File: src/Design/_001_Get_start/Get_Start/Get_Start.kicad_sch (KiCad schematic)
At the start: 7 parts, among them SW1 SW_SPST

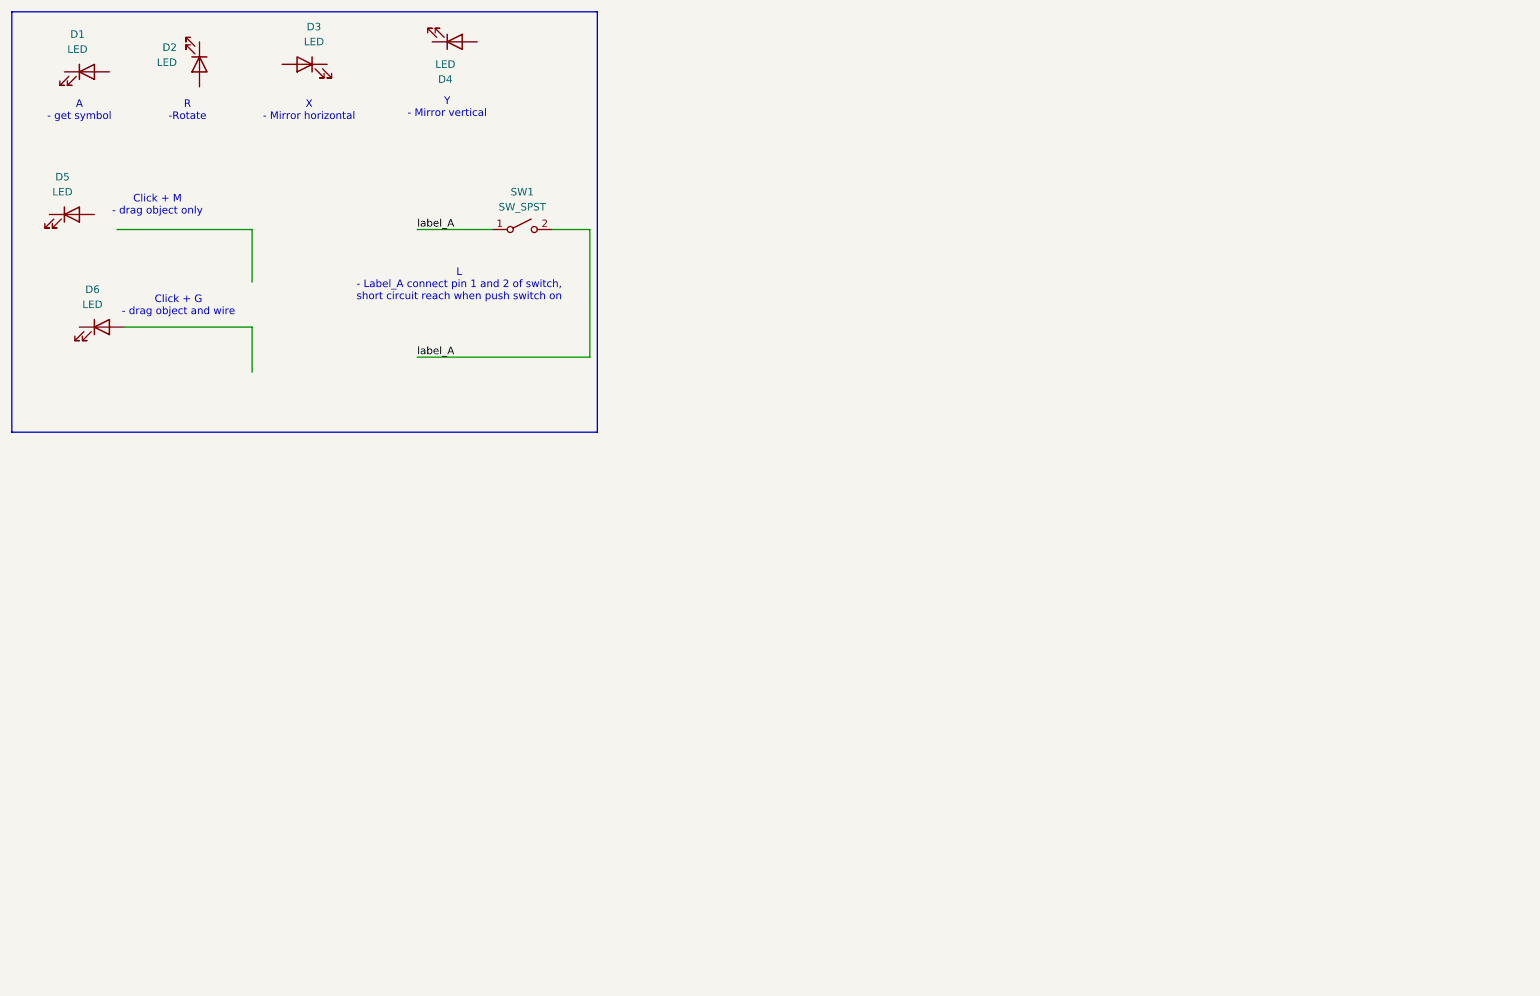
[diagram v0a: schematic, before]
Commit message: :bookmark_tabs: Note something schematic - 001: special connect hierarchy of sheets - 003: Set properties for symbols - 004: error rule check for schematic
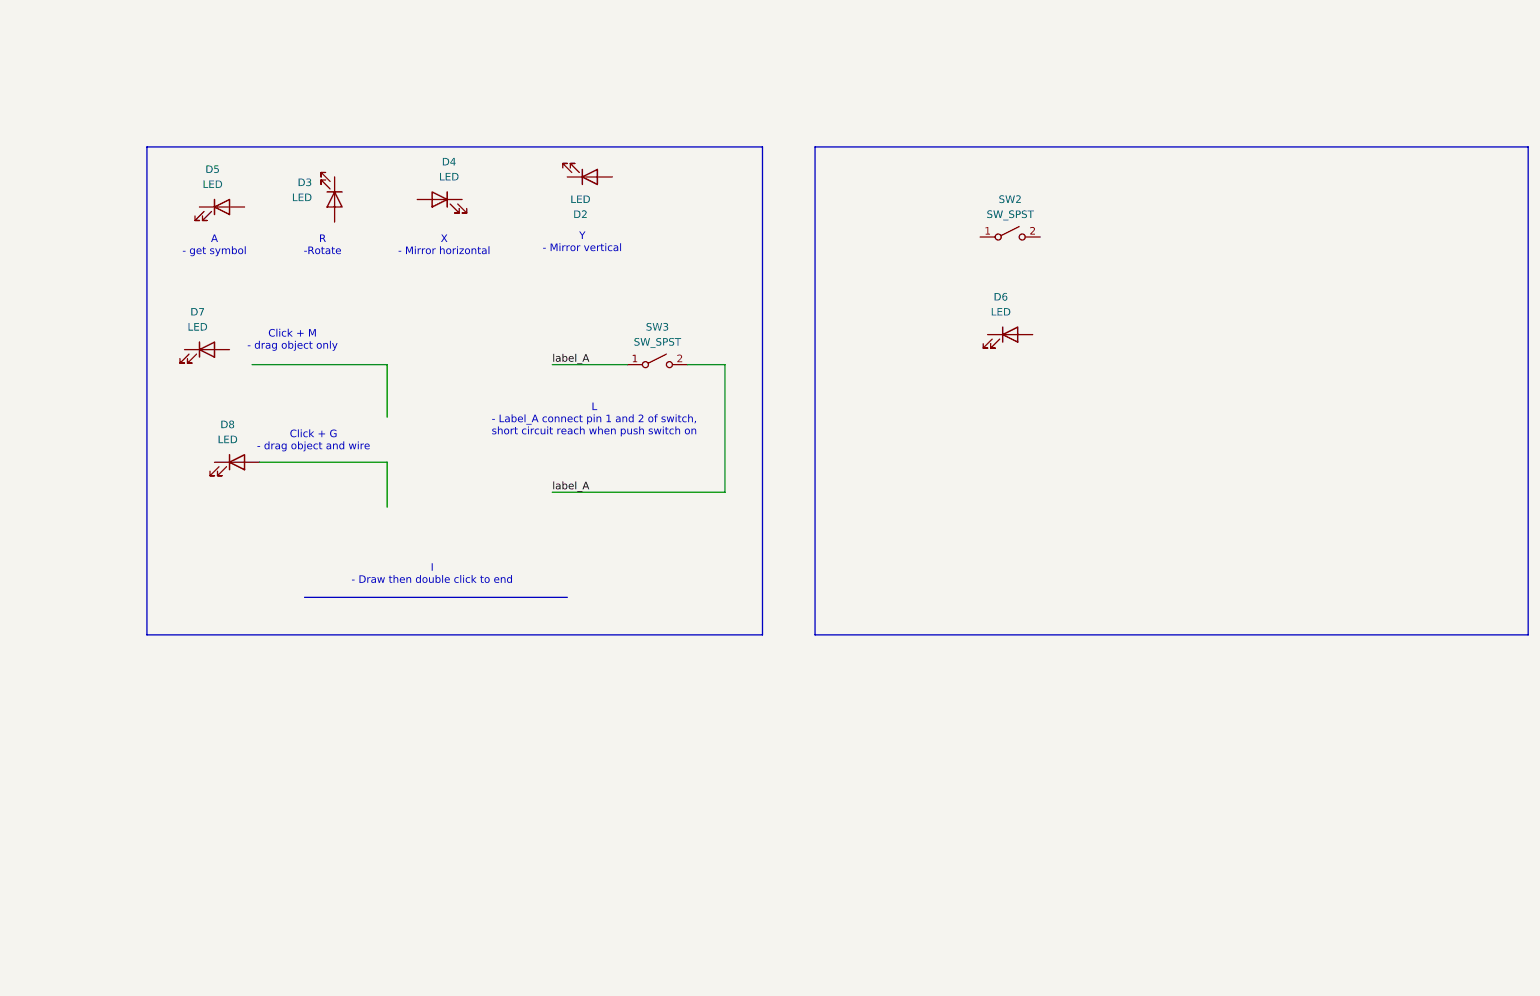
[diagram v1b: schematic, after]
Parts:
- added D6: LED, symbol Device:LED
- added SW2: SW_SPST, symbol Switch:SW_SPST
- renumbered D4 to D2, D2 to D3, D3 to D4, D1 to D5, D5 to D7, D6 to D8, SW1 to SW3
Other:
- note added: "I - Draw then double click to end"
- moved on the sheet: D2, D3, D4, D5, D7, D8, SW3

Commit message: update
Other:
- added sheet Sheet child 1 (Sheet_child_1.kicad_sch)
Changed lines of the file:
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@@
-		)
-	)
-	(rule_area
-		(polyline
-			(pts
-				(xy 246.38 43.18) (xy 215.9 43.18) (xy 215.9 62.23) (xy 223.52 69.85) (xy 243.84 69.85) (xy 251.46 62.23)
-				(xy 251.46 48.26)
-			)
-			(stroke
-				(width 0)
-				(type dash)
-			)
-			(fill
-				(type none)
-			)
 		)
 	)
@@
 				)
 			)
+		)
+	)
+	(sheet
+		(at 36.83 137.16)
+		(size 49.53 33.02)
+		(exclude_from_sim no)
+		(in_bom yes)
+		(on_board yes)
+		(dnp no)
+		(fields_autoplaced yes)
+		(stroke
+			(width 0.1524)
+			(type solid)
+		)
+		(fill
+			(color 0 0 0 0.0000)
+		)
+		(property "Sheetname" "Sheet child 1"
+			(at 36.83 136.4484 0)
+			(effects
+				(font
+					(size 1.27 1.27)
+				)
+				(justify left bottom)
+			)
+		)
+		(property "Sheetfile" "Sheet_child_1.kicad_sch"
+			(at 36.83 170.7646 0)
+			(effects
+				(font
+					(size 1.27 1.27)
+				)
+				(justify left top)
+			)
+		)
+		(pin "hierar_1" input
+			(at 86.36 143.51 0)
+			(effects
+				(font
+					(size 1.27 1.27)
+				)
+				(justify right)
+			)
+		)
+		(pin "hierar_2" input
+			(at 74.93 170.18 270)
+			(effects
+				(font
+					(size 1.27 1.27)
+				)
+				(justify left)
+			)
+		)
+		(instances
+			(project "Get_Start"
+				(path "/3c26b505-18dc-433f-8569-20dcedbd6448"
+					(page "2")
+				)
+			)

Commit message: reup
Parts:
- removed D6: LED, symbol Device:LED
- removed SW2: SW_SPST, symbol Switch:SW_SPST
- added D5: LED, symbol Device:LED
- renumbered D2 to D1, D3 to D2, D4 to D3, D5 to D4, D7 to D6, D8 to D7, SW3 to SW1
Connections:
- new net null: D5.1 (K), D5.2 (A)
- no-connect marks 0 -> 16
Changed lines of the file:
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@@
+		)
+	)
+	(no_connect
+		(at 106.68 40.64)
+	)
+	(no_connect
+		(at 67.31 48.26)
+	)
+	(no_connect
+		(at 76.2 96.52)
+	)
+	(no_connect
+		(at 81.28 44.45)
+	)
+	(no_connect
+		(at 52.07 45.72)
+	)
+	(no_connect
+		(at 53.34 72.39)
+	)
+	(no_connect
+		(at 67.31 40.64)
+	)
+	(no_connect
+		(at 49.53 69.85)
+	)
+	(no_connect
+		(at 114.3 40.64)
+	)
+	(no_connect
+		(at 44.45 45.72)
+	)
+	(no_connect
+		(at 41.91 69.85)
+	)
+	(no_connect
+		(at 88.9 44.45)
+	)
+	(no_connect
+		(at 46.99 88.9)
+	)
+	(no_connect
+		(at 76.2 81.28)
+	)
+	(no_connect
+		(at 92.71 143.51)
+	)
+	(no_connect
+		(at 74.93 176.53)
+	)
+	(wire
+		(pts
+			(xy 165.1 50.8) (xy 168.91 50.8)
+		)
+		(stroke
+			(width 0)
+			(type default)
+		)
+	)
+	(wire
+		(pts
+			(xy 74.93 170.18) (xy 74.93 176.53)
+		)
+		(stroke
+			(width 0)
+			(type default)
 		)
 	)
@@
 	(wire
 		(pts
+			(xy 176.53 50.8) (xy 179.07 50.8)
+		)
+		(stroke
+			(width 0)
+			(type default)
+		)
+	)
+	(wire
+		(pts
 			(xy 133.35 93.98) (xy 133.35 72.39)
 		)
@@
 	(wire
 		(pts
+			(xy 86.36 143.51) (xy 92.71 143.51)
+		)
+		(stroke
+			(width 0)
+			(type default)
+		)
+	)
+	(wire
+		(pts
 			(xy 104.14 72.39) (xy 116.84 72.39)
 		)
@@
 			(width 0)
 			(type default)
+		)
+	)
+	(label "null2"
+		(at 76.2 76.2 0)
+		(effects
+			(font
+				(size 1.27 1.27)
+			)
+			(justify left bottom)
+		)
+	)
+	(label "null"
+		(at 179.07 50.8 0)
+		(effects
+			(font
+				(size 1.27 1.27)
+			)
+			(justify left bottom)
+		)
+	)
+	(label "null"
+		(at 57.15 72.39 0)
+		(effects
+			(font
+				(size 1.27 1.27)
+			)
+			(justify left bottom)
 		)
 	)
@@
 			)
 			(justify left bottom)
+		)
+	)
+	(label "null2"
+		(at 165.1 50.8 180)
+		(effects
+			(font
+				(size 1.27 1.27)
+			)
+			(justify right bottom)
 		)
 	)
@@
 		(on_board yes)
 		(dnp no)
-		(property "Reference" "D3"
+		(property "Reference" "D2"
 			(at 63.5 41.5924 90)
 			(effects
@@
 			(project ""
 				(path "/3c26b505-18dc-433f-8569-20dcedbd6448"
-					(reference "D3")
+					(reference "D2")
 					(unit 1)
 				)
@@
 		(on_board yes)
 		(dnp no)
-		(property "Reference" "D4"
+		(property "Reference" "D3"
 			(at 86.6775 38.1 0)
 			(effects
@@
 			(project ""
 				(path "/3c26b505-18dc-433f-8569-20dcedbd6448"
-					(reference "D4")
+					(reference "D3")
 					(unit 1)
 				)
@@
 		(on_board yes)
 		(dnp no)
-		(fields_autoplaced yes)
-		(property "Reference" "D8"
+		(property "Reference" "D7"
 			(at 49.2125 82.55 0)
 			(effects
@@
 			(project ""
 				(path "/3c26b505-18dc-433f-8569-20dcedbd6448"
-					(reference "D8")
+					(reference "D7")
 					(unit 1)
 				)
@@
 		(on_board yes)
 		(dnp no)
-		(property "Reference" "D2"
+		(property "Reference" "D1"
 			(at 108.9025 46.99 0)
 			(effects
@@
 			(project "Get_Start"
 				(path "/3c26b505-18dc-433f-8569-20dcedbd6448"
-					(reference "D2")
+					(reference "D1")
 					(unit 1)
 				)
@@
 		(dnp no)
 		(fields_autoplaced yes)
-		(property "Reference" "D7"
+		(property "Reference" "D6"
 			(at 44.1325 63.5 0)
 			(effects
@@
 			(project ""
 				(path "/3c26b505-18dc-433f-8569-20dcedbd6448"
-					(reference "D7")
+					(reference "D6")
+					(unit 1)
+				)
+			)
+		)
+	)
+	(symbol
+		(lib_id "Device:LED")
+		(at 172.72 50.8 0)
+		(unit 1)
+		(exclude_from_sim no)
+		(in_bom yes)
+		(on_board yes)
+		(dnp no)
+		(fields_autoplaced yes)
+		(property "Reference" "D5"
+			(at 171.1325 44.45 0)
+			(effects
+				(font
+					(size 1.27 1.27)
+				)
+			)
+		)
+		(property "Value" "LED"
+			(at 171.1325 46.99 0)
+			(effects
+				(font
+					(size 1.27 1.27)
+				)
+			)
+		)
+		(property "Footprint" ""
+			(at 172.72 50.8 0)
+			(effects
+				(font
+					(size 1.27 1.27)
+				)
+				(hide yes)
+			)
+		)
+		(property "Datasheet" "~"
+			(at 172.72 50.8 0)
+			(effects
+				(font
+					(size 1.27 1.27)
+				)
+				(hide yes)
+			)
+		)
+		(property "Description" "Light emitting diode"
+			(at 172.72 50.8 0)
+			(effects
+				(font
+					(size 1.27 1.27)
+				)
+				(hide yes)
+			)
+		)
+		(property "Sim.Pins" "1=K 2=A"
+			(at 172.72 50.8 0)
+			(effects
+				(font
+					(size 1.27 1.27)
+				)
+				(hide yes)
+			)
+		)
+		(pin "2"
+		)
+		(pin "1"
+		)
+		(instances
+			(project ""
+				(path "/3c26b505-18dc-433f-8569-20dcedbd6448"
+					(reference "D5")
 					(unit 1)
 				)
@@
 		(dnp no)
 		(fields_autoplaced yes)
-		(property "Reference" "D5"
+		(property "Reference" "D4"
 			(at 46.6725 39.37 0)
 			(effects
@@
 			(project ""
 				(path "/3c26b505-18dc-433f-8569-20dcedbd6448"
-					(reference "D5")
+					(reference "D4")
 					(unit 1)
 				)
@@
 		(dnp no)
 		(fields_autoplaced yes)
-		(property "Reference" "SW3"
+		(property "Reference" "SW1"
 			(at 121.92 66.04 0)
 			(effects
@@
 			(project ""
 				(path "/3c26b505-18dc-433f-8569-20dcedbd6448"
-					(reference "SW3")
-					(unit 1)
-				)
-			)
-		)
-	)
-	(symbol
-		(lib_id "Device:LED")
-		(at 181.61 67.31 0)
-		(unit 1)
-		(exclude_from_sim no)
-		(in_bom yes)
-		(on_board yes)
-		(dnp no)
-		(fields_autoplaced yes)
-		(property "Reference" "D6"
-			(at 180.0225 60.96 0)
-			(effects
-				(font
-					(size 1.27 1.27)
-				)
-			)
-		)
-		(property "Value" "LED"
-			(at 180.0225 63.5 0)
-			(effects
-				(font
-					(size 1.27 1.27)
-				)
-			)
-		)
-		(property "Footprint" ""
-			(at 181.61 67.31 0)
-			(effects
-				(font
-					(size 1.27 1.27)
-				)
-				(hide yes)
-			)
-		)
-		(property "Datasheet" "~"
-			(at 181.61 67.31 0)
-			(effects
-				(font
-					(size 1.27 1.27)
-				)
-				(hide yes)
-			)
-		)
-		(property "Description" "Light emitting diode"
-			(at 181.61 67.31 0)
-			(effects
-				(font
-					(size 1.27 1.27)
-				)
-				(hide yes)
-			)
-		)
-		(property "Sim.Pins" "1=K 2=A"
-			(at 181.61 67.31 0)
-			(effects
-				(font
-					(size 1.27 1.27)
-				)
-				(hide yes)
-			)
-		)
-		(pin "1"
-		)
-		(pin "2"
-		)
-		(instances
-			(project ""
-				(path "/3c26b505-18dc-433f-8569-20dcedbd6448"
-					(reference "D6")
-					(unit 1)
-				)
-			)
-		)
-	)
-	(symbol
-		(lib_id "Switch:SW_SPST")
-		(at 181.61 50.8 0)
-		(unit 1)
-		(exclude_from_sim no)
-		(in_bom yes)
-		(on_board yes)
-		(dnp no)
-		(fields_autoplaced yes)
-		(property "Reference" "SW2"
-			(at 181.61 44.45 0)
-			(effects
-				(font
-					(size 1.27 1.27)
-				)
-			)
-		)
-		(property "Value" "SW_SPST"
-			(at 181.61 46.99 0)
-			(effects
-				(font
-					(size 1.27 1.27)
-				)
-			)
-		)
-		(property "Footprint" ""
-			(at 181.61 50.8 0)
-			(effects
-				(font
-					(size 1.27 1.27)
-				)
-				(hide yes)
-			)
-		)
-		(property "Datasheet" "~"
-			(at 181.61 50.8 0)
-			(effects
-				(font
-					(size 1.27 1.27)
-				)
-				(hide yes)
-			)
-		)
-		(property "Description" "Single Pole Single Throw (SPST) switch"
-			(at 181.61 50.8 0)
-			(effects
-				(font
-					(size 1.27 1.27)
-				)
-				(hide yes)
-			)
-		)
-		(pin "1"
-		)
-		(pin "2"
-		)
-		(instances
-			(project ""
-				(path "/3c26b505-18dc-433f-8569-20dcedbd6448"
-					(reference "SW2")
+					(reference "SW1")
 					(unit 1)
 				)
@@
 			)
 		)
-		(pin "hierar_1" input
+		(pin "hierar_1" output
 			(at 86.36 143.51 0)
 			(effects
@@
 			)
 		)
-		(pin "hierar_2" input
+		(pin "hierar_2" output
 			(at 74.93 170.18 270)
 			(effects

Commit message: :gear: pre setup pcb - number of copper layer - board layer - design rule
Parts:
- added SW2: 100 abc, Simple_test_library:First component, symbol Simple_test_Library:Switch
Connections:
- net null: no longer names the net of D5.1 (K)
- net null: no longer D5.2 (A)
- no-connect marks 16 -> 21
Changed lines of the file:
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@@
+	)
+	(no_connect
+		(at 161.29 76.2)
 	)
 	(no_connect
@@
 	)
 	(no_connect
+		(at 161.29 78.74)
+	)
+	(no_connect
 		(at 76.2 96.52)
 	)
@@
 	)
 	(no_connect
-		(at 53.34 72.39)
-	)
-	(no_connect
 		(at 67.31 40.64)
 	)
 	(no_connect
+		(at 161.29 73.66)
+	)
+	(no_connect
+		(at 165.1 50.8)
+	)
+	(no_connect
 		(at 49.53 69.85)
 	)
 	(no_connect
+		(at 186.69 50.8)
+	)
+	(no_connect
 		(at 114.3 40.64)
 	)
 	(no_connect
+		(at 173.99 76.2)
+	)
+	(no_connect
 		(at 44.45 45.72)
 	)
@@
 	)
 	(no_connect
+		(at 173.99 73.66)
+	)
+	(no_connect
 		(at 46.99 88.9)
 	)
 	(no_connect
-		(at 76.2 81.28)
-	)
-	(no_connect
 		(at 92.71 143.51)
 	)
@@
 	(wire
 		(pts
-			(xy 53.34 72.39) (xy 76.2 72.39)
-		)
-		(stroke
-			(width 0)
-			(type default)
-		)
-	)
-	(wire
-		(pts
-			(xy 76.2 72.39) (xy 76.2 81.28)
-		)
-		(stroke
-			(width 0)
-			(type default)
-		)
-	)
-	(wire
-		(pts
-			(xy 176.53 50.8) (xy 179.07 50.8)
-		)
-		(stroke
-			(width 0)
-			(type default)
-		)
-	)
-	(wire
-		(pts
 			(xy 133.35 93.98) (xy 133.35 72.39)
 		)
@@
 		)
 	)
+	(wire
+		(pts
+			(xy 176.53 50.8) (xy 186.69 50.8)
+		)
+		(stroke
+			(width 0)
+			(type default)
+		)
+	)
 	(polyline
 		(pts
@@
 			(width 0)
 			(type default)
-		)
-	)
-	(label "null2"
-		(at 76.2 76.2 0)
-		(effects
-			(font
-				(size 1.27 1.27)
-			)
-			(justify left bottom)
-		)
-	)
-	(label "null"
-		(at 179.07 50.8 0)
-		(effects
-			(font
-				(size 1.27 1.27)
-			)
-			(justify left bottom)
-		)
-	)
-	(label "null"
-		(at 57.15 72.39 0)
-		(effects
-			(font
-				(size 1.27 1.27)
-			)
-			(justify left bottom)
 		)
 	)
@@
 			)
 			(justify left bottom)
-		)
-	)
-	(label "null2"
-		(at 165.1 50.8 180)
-		(effects
-			(font
-				(size 1.27 1.27)
-			)
-			(justify right bottom)
 		)
 	)
@@
 		(dnp no)
 		(property "Reference" "D2"
-			(at 63.5 41.5924 90)
-			(effects
-				(font
-					(size 1.27 1.27)
-				)
-				(justify right)
+			(at 69.85 44.45 0)
+			(effects
+				(font
+					(size 1.27 1.27)
+				)
 			)
 		)
 		(property "Value" "LED"
-			(at 63.5 44.1324 90)
-			(effects
-				(font
-					(size 1.27 1.27)
-				)
-				(justify right)
+			(at 64.77 44.45 0)
+			(effects
+				(font
+					(size 1.27 1.27)
+				)
 			)
 		)
@@
 		(dnp no)
 		(property "Reference" "D3"
-			(at 86.6775 38.1 0)
+			(at 85.09 41.91 0)
 			(effects
 				(font
@@
 		)
 		(property "Value" "LED"
-			(at 86.6775 40.64 0)
+			(at 85.09 46.99 0)
 			(effects
 				(font
@@
 		(dnp no)
 		(property "Reference" "D7"
-			(at 49.2125 82.55 0)
+			(at 50.8 86.36 0)
 			(effects
 				(font
@@
 		)
 		(property "Value" "LED"
-			(at 49.2125 85.09 0)
+			(at 50.8 91.44 0)
 			(effects
 				(font
@@
 		(dnp no)
 		(property "Reference" "D1"
-			(at 108.9025 46.99 0)
+			(at 110.49 43.18 0)
 			(effects
 				(font
@@
 		)
 		(property "Value" "LED"
-			(at 108.9025 44.45 0)
+			(at 110.49 38.1 0)
 			(effects
 				(font
@@
 					(unit 1)
 				)
+			)
+		)
+	)
+	(symbol
+		(lib_id "Simple_test_Library:Switch")
+		(at 167.64 71.12 0)
+		(unit 1)
+		(exclude_from_sim no)
+		(in_bom yes)
+		(on_board yes)
+		(dnp no)
+		(property "Reference" "SW2"
+			(at 164.846 68.326 0)
+			(effects
+				(font
+					(size 1.27 1.27)
+					(thickness 0.254)
+					(bold yes)
+				)
+			)
+		)
+		(property "Value" "100 abc"
+			(at 167.64 70.104 0)
+			(effects
+				(font
+					(size 1.27 1.27)
+				)
+			)
+		)
+		(property "Footprint" "Simple_test_library:First component"
+			(at 168.402 64.516 0)
+			(effects
+				(font
+					(size 1.27 1.27)
+				)
+				(hide yes)
+			)
+		)
+		(property "Datasheet" ""
+			(at 167.64 71.12 0)
+			(effects
+				(font
+					(size 1.27 1.27)
+				)
+				(hide yes)
+			)
+		)
+		(property "Description" "This is detailed description for test symbol"
+			(at 168.91 61.722 0)
+			(effects
+				(font
+					(size 1.27 1.27)
+					(color 255 61 68 1)
+				)
+				(hide yes)
+			)
+		)
+		(pin "3"
+		)
+		(pin "4"
+		)
+		(pin "2"
+		)
+		(pin "1"
+		)
+		(pin "5"
+		)
+		(instances
+			(project ""
+				(path "/3c26b505-18dc-433f-8569-20dcedbd6448"
+					(reference "SW2")
+					(unit 1)
+				)
